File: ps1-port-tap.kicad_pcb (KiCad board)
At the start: 2 copper layers, 40 x 51 mm, 19 parts, among them J1 CONSOLE, J2 DEVICE, J3 LA_TAP

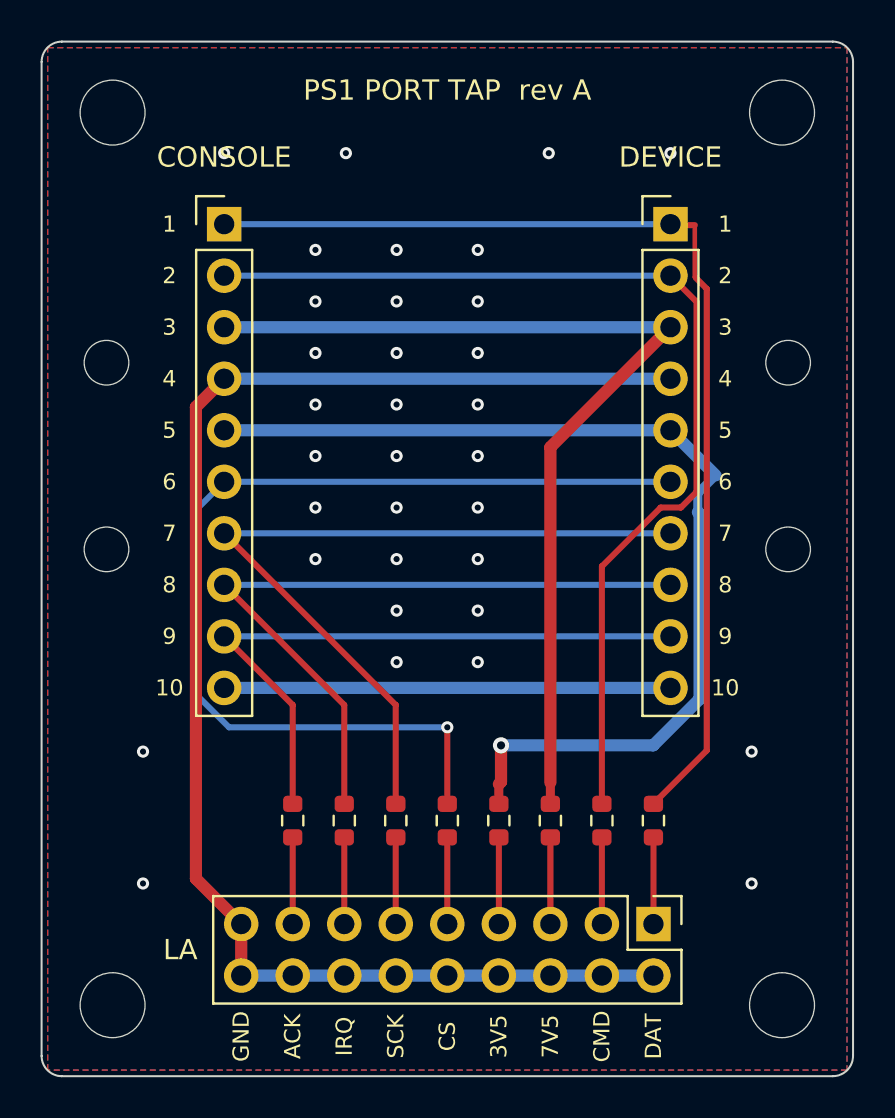
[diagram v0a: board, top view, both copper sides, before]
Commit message: Hand-route every run straight, keep pour out of pad rows
Freerouting left 90-degree points, sub-width jogs and necked traces that DRC
passes. Routing is now scripted and straight, the pour stops at the pad rows,
and tools/check_geometry.py plus zoomed crops gate the build.
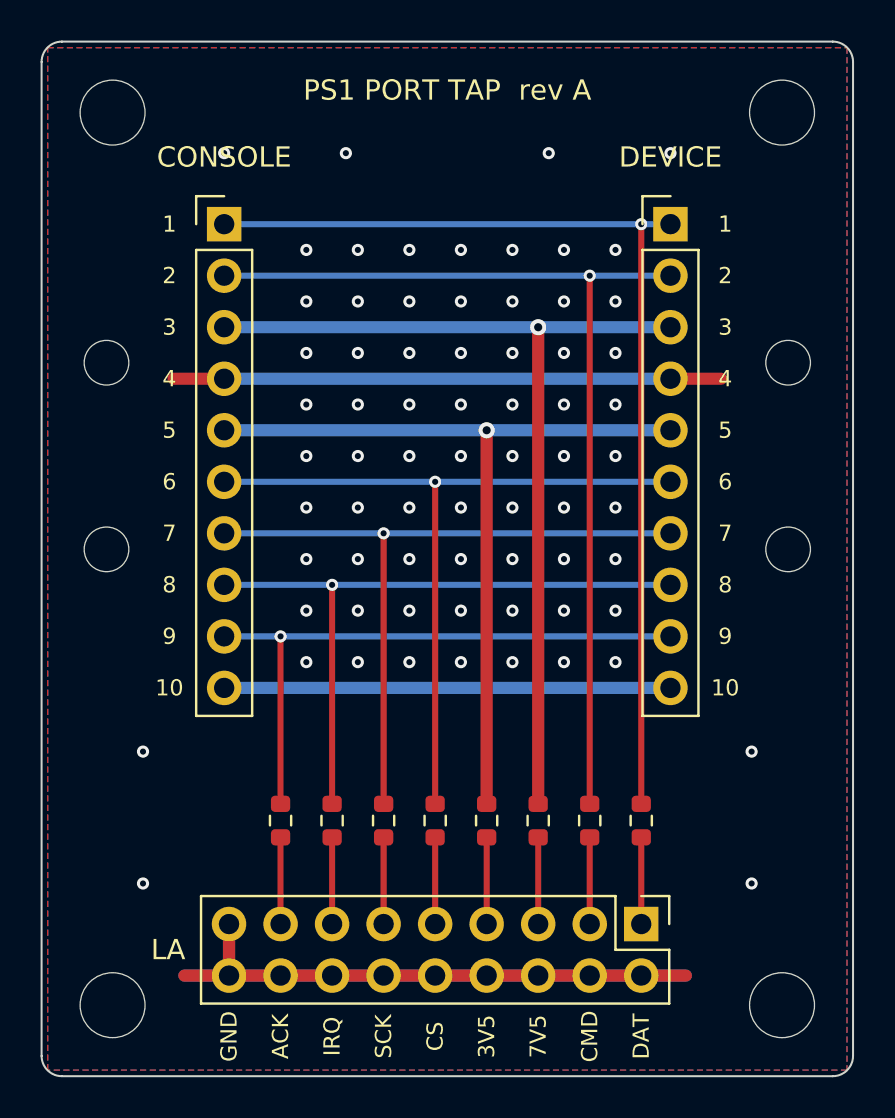
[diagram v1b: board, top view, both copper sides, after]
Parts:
- moved R2 0.60 mm to (127.0, 138.4)
- moved R4 0.60 mm to (121.9, 138.4)
- moved R7 0.60 mm to (114.3, 138.4)
- moved J3 0.60 mm to (129.6, 143.5)
- moved R1 0.60 mm to (129.6, 138.4)
- moved R3 0.60 mm to (124.5, 138.4)
- moved R5 0.60 mm to (119.4, 138.4)
- moved R6 0.60 mm to (116.9, 138.4)
- moved R8 0.60 mm to (111.8, 138.4)
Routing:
- net /~{CS}: track 49.8 -> 37.9 mm
- net /+3V5: track 50.2 -> 40.4 mm
- net /GND: track 73.2 -> 81.5 mm, vias 33 -> 71
- net /SCK: track 38.8 -> 35.3 mm, vias 0 -> 1
- net /CMD: track 51.1 -> 48.0 mm, vias 0 -> 1
- net /DAT: track 53.1 -> 50.6 mm, vias 0 -> 1
- net /~{IRQ}: track 35.2 -> 32.8 mm, vias 0 -> 1
- net /+7V5: track 47.9 -> 45.5 mm, vias 0 -> 1
- net /~{ACK}: track 31.7 -> 30.3 mm, vias 0 -> 1
